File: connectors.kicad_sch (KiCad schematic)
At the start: 16 parts

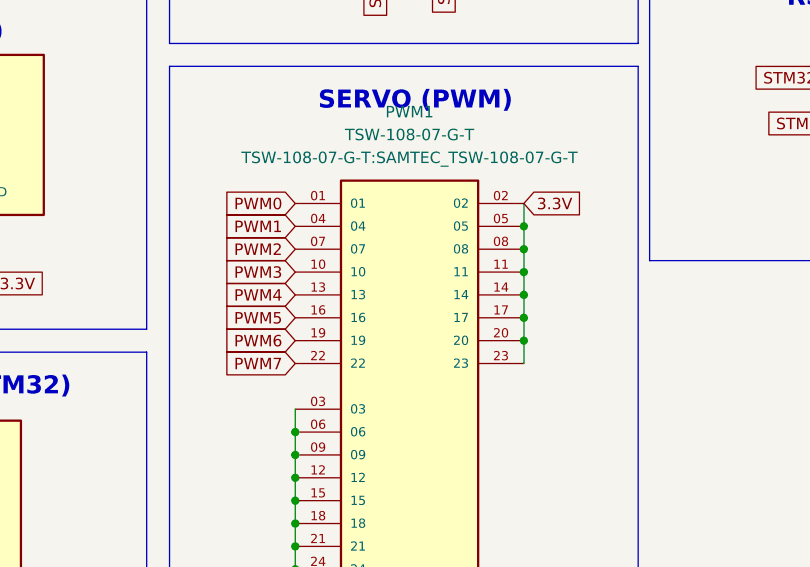
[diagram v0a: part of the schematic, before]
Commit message: grouped components
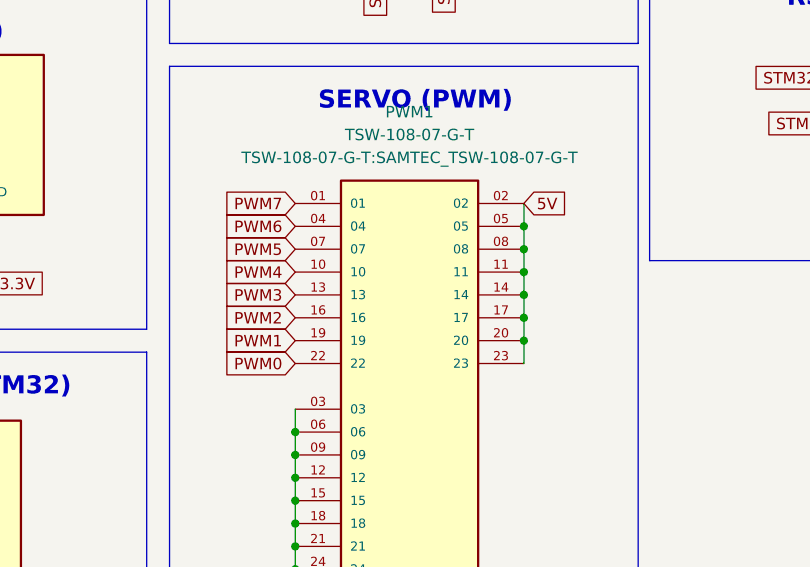
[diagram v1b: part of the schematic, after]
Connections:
- net 3.3V: no longer PWM1.02, PWM1.05, PWM1.08, PWM1.11, PWM1.14, PWM1.17, PWM1.20, PWM1.23
- net 5V: now also PWM1.02, PWM1.05, PWM1.08, PWM1.11, PWM1.14, PWM1.17, PWM1.20, PWM1.23
- net PWM0: now also PWM1.22; no longer PWM1.01
- net PWM1: now also PWM1.19; no longer PWM1.04
- net PWM2: now also PWM1.16; no longer PWM1.07
- net PWM3: now also PWM1.13; no longer PWM1.10
- net PWM4: now also PWM1.10; no longer PWM1.13
- net PWM5: now also PWM1.07; no longer PWM1.16
- net PWM6: now also PWM1.04; no longer PWM1.19
- net PWM7: now also PWM1.01; no longer PWM1.22

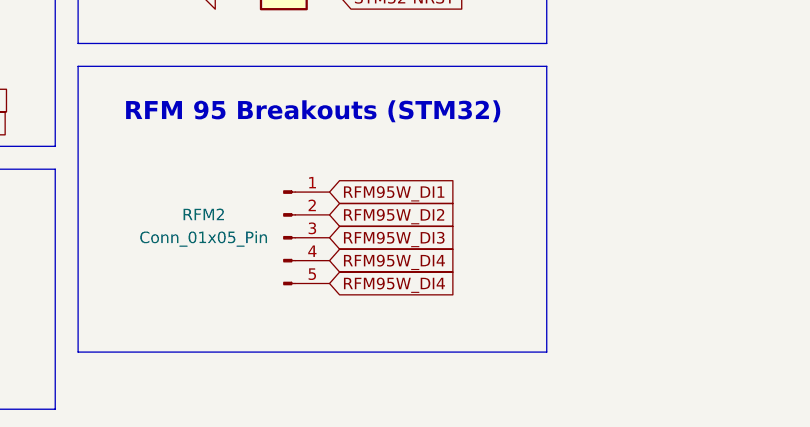
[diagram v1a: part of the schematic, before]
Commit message: updated tracks
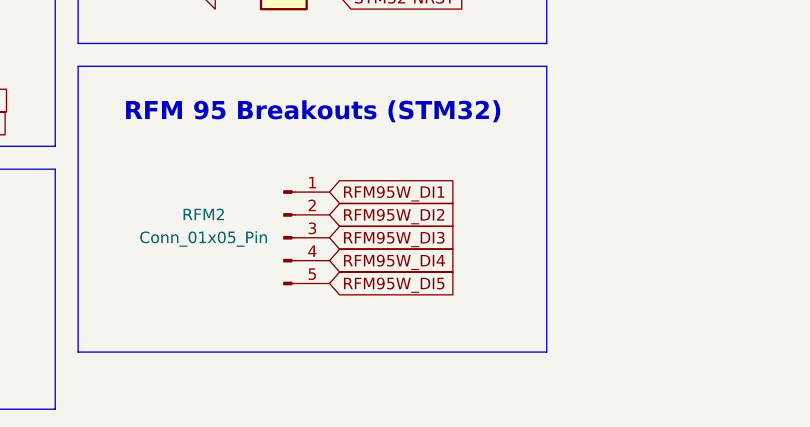
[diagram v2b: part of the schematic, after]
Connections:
- net RFM95W_DI4: no longer RFM2.5 (Pin_5)
- new net RFM95W_DI5: RFM2.5 (Pin_5)
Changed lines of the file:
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@@
     )
   )
-  (global_label "RFM95W_DI4" (shape input) (at 97.79 181.61 0) (fields_autoplaced)
+  (global_label "RFM95W_DI5" (shape input) (at 97.79 181.61 0) (fields_autoplaced)
     (effects (font (size 1.27 1.27)) (justify left))
     (property "Intersheetrefs" "${INTERSHEET_REFS}" (at 112.5075 181.61 0)

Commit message: started routing
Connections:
- net PWM0: now also PWM1.01; no longer PWM1.22
- net PWM1: now also PWM1.04; no longer PWM1.19
- net PWM2: now also PWM1.07; no longer PWM1.16
- net PWM3: now also PWM1.10; no longer PWM1.13
- net PWM4: now also PWM1.13; no longer PWM1.10
- net PWM5: now also PWM1.16; no longer PWM1.07
- net PWM6: now also PWM1.19; no longer PWM1.04
- net PWM7: now also PWM1.22; no longer PWM1.01
- net RFM95W_DI1: now also RFM2.5 (Pin_5); no longer RFM2.1 (Pin_1)
- net RFM95W_DI2: now also RFM2.4 (Pin_4); no longer RFM2.2 (Pin_2)
- net RFM95W_DI4: now also RFM2.2 (Pin_2); no longer RFM2.4 (Pin_4)
- net RFM95W_DI5: now also RFM2.1 (Pin_1); no longer RFM2.5 (Pin_5)
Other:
- moved on the sheet: RFM2

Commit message: more routing
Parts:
- added J2: Screw_Terminal_01x04, TerminalBlock_TE-Connectivity:TerminalBlock_TE_282834-4_1x04_P2.54mm_Horizontal, symbol Connector:Screw_Terminal_01x04
- added RFM3: Conn_01x05_Pin, Connector_PinHeader_1.27mm:PinHeader_1x05_P1.27mm_Vertical, symbol Connector:Conn_01x05_Pin
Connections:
- new net GPS_INT: RFM3.4 (Pin_4)
- new net GPS_RST: RFM3.3 (Pin_3)
- new net GPS_RX: RFM3.1 (Pin_1)
- new net GPS_SAFE: RFM3.5 (Pin_5)
- new net GPS_TX: RFM3.2 (Pin_2)
- new net PYRO-TERM_A: J2.1 (Pin_1)
- new net PYRO-TERM_B: J2.2 (Pin_2)
- new net PYRO-TERM_C: J2.3 (Pin_3)
- new net PYRO-TERM_D: J2.4 (Pin_4)
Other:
- note added: "GPS Breakouts"
- note added: "PYRO (STM32)"
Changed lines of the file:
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@@
+    (fill (type none))
+  )
+  (rectangle (start 124.46 124.46) (end 176.53 156.21)
+    (stroke (width 0) (type default))
     (fill (type none))
   )
@@
     (fill (type none))
   )
+  (rectangle (start 124.46 83.82) (end 185.42 121.92)
+    (stroke (width 0) (type default))
+    (fill (type none))
+  )
   (rectangle (start 69.85 60.96) (end 121.92 121.92)
     (stroke (width 0) (type default))
@@
     (effects (font (size 2 2) (thickness 0.8) bold) (justify left bottom))
   )
+  (text "PYRO (STM32)" (at 138.43 90.17 0)
+    (effects (font (size 2 2) (thickness 0.8) bold) (justify left bottom))
+  )
   (text "SWD Connector (STM32)" (at 78.74 129.54 0)
     (effects (font (size 2 2) (thickness 0.8) bold) (justify left bottom))
@@
     (effects (font (size 1.27 1.27) bold) (justify left bottom))
   )
+  (text "GPS Breakouts\n" (at 138.43 129.54 0)
+    (effects (font (size 2 2) (thickness 0.8) bold) (justify left bottom))
+  )
   (text "RFD UART 1 (STM32)" (at 26.67 97.79 0)
     (effects (font (size 2 2) (thickness 0.8) bold) (justify left bottom))
@@
     )
   )
+  (global_label "GPS_RX" (shape input) (at 149.86 134.62 0) (fields_autoplaced)
+    (effects (font (size 1.27 1.27)) (justify left))
+    (property "Intersheetrefs" "${INTERSHEET_REFS}" (at 160.0418 134.62 0)
+      (effects (font (size 1.27 1.27)) (justify left) hide)
+    )
+  )
   (global_label "ESP32-I2C1_SCL" (shape input) (at 41.91 86.36 180) (fields_autoplaced)
     (effects (font (size 1.27 1.27)) (justify right))
@@
     )
   )
+  (global_label "GPS_TX" (shape input) (at 149.86 137.16 0) (fields_autoplaced)
+    (effects (font (size 1.27 1.27)) (justify left))
+    (property "Intersheetrefs" "${INTERSHEET_REFS}" (at 159.7394 137.16 0)
+      (effects (font (size 1.27 1.27)) (justify left) hide)
+    )
+  )
   (global_label "INA219_SCL" (shape input) (at 251.46 53.34 0) (fields_autoplaced)
     (effects (font (size 1.27 1.27)) (justify left))
@@
     )
   )
+  (global_label "GPS_SAFE" (shape input) (at 149.86 144.78 0) (fields_autoplaced)
+    (effects (font (size 1.27 1.27)) (justify left))
+    (property "Intersheetrefs" "${INTERSHEET_REFS}" (at 162.098 144.78 0)
+      (effects (font (size 1.27 1.27)) (justify left) hide)
+    )
+  )
+  (global_label "PYRO-TERM_C" (shape input) (at 152.4 102.87 180) (fields_autoplaced)
+    (effects (font (size 1.27 1.27)) (justify right))
+    (property "Intersheetrefs" "${INTERSHEET_REFS}" (at 135.8077 102.87 0)
+      (effects (font (size 1.27 1.27)) (justify right) hide)
+    )
+  )
   (global_label "ESP32_RFD900_TX" (shape input) (at 40.64 148.59 180) (fields_autoplaced)
     (effects (font (size 1.27 1.27)) (justify right))
@@
     )
   )
+  (global_label "PYRO-TERM_A" (shape input) (at 152.4 97.79 180) (fields_autoplaced)
+    (effects (font (size 1.27 1.27)) (justify right))
+    (property "Intersheetrefs" "${INTERSHEET_REFS}" (at 135.9891 97.79 0)
+      (effects (font (size 1.27 1.27)) (justify right) hide)
+    )
+  )
   (global_label "H3LIS331DL_SDO" (shape input) (at 255.27 106.68 0) (fields_autoplaced)
     (effects (font (size 1.27 1.27)) (justify left))
@@
     )
   )
+  (global_label "PYRO-TERM_B" (shape input) (at 152.4 100.33 180) (fields_autoplaced)
+    (effects (font (size 1.27 1.27)) (justify right))
+    (property "Intersheetrefs" "${INTERSHEET_REFS}" (at 135.8077 100.33 0)
+      (effects (font (size 1.27 1.27)) (justify right) hide)
+    )
+  )
   (global_label "SD_CS" (shape input) (at 255.27 135.89 0) (fields_autoplaced)
     (effects (font (size 1.27 1.27)) (justify left))
@@
     )
   )
+  (global_label "GPS_INT" (shape input) (at 149.86 142.24 0) (fields_autoplaced)
+    (effects (font (size 1.27 1.27)) (justify left))
+    (property "Intersheetrefs" "${INTERSHEET_REFS}" (at 160.4652 142.24 0)
+      (effects (font (size 1.27 1.27)) (justify left) hide)
+    )
+  )
   (global_label "STM32-SPI2_CS0" (shape input) (at 250.19 124.46 180) (fields_autoplaced)
     (effects (font (size 1.27 1.27)) (justify right))
@@
     )
   )
+  (global_label "PYRO-TERM_D" (shape input) (at 152.4 105.41 180) (fields_autoplaced)
+    (effects (font (size 1.27 1.27)) (justify right))
+    (property "Intersheetrefs" "${INTERSHEET_REFS}" (at 135.8077 105.41 0)
+      (effects (font (size 1.27 1.27)) (justify right) hide)
+    )
+  )
   (global_label "5V" (shape input) (at 40.64 105.41 180) (fields_autoplaced)
     (effects (font (size 1.27 1.27)) (justify right))
@@
     (property "Intersheetrefs" "${INTERSHEET_REFS}" (at 233.1745 158.75 0)
       (effects (font (size 1.27 1.27)) (justify right) hide)
+    )
+  )
+  (global_label "GPS_RST" (shape input) (at 149.86 139.7 0) (fields_autoplaced)
+    (effects (font (size 1.27 1.27)) (justify left))
+    (property "Intersheetrefs" "${INTERSHEET_REFS}" (at 161.0094 139.7 0)
+      (effects (font (size 1.27 1.27)) (justify left) hide)
     )
   )
@@
         (path "/e12346fa-509d-4de9-8ab1-dced307292db/7d58c90a-6730-4b63-ae17-c9d1fe4b2f54"
           (reference "#PWR0166") (unit 1)
+        )
+      )
+    )
+  )
+  (symbol (lib_id "Connector:Conn_01x05_Pin") (at 144.78 139.7 0) (unit 1)
+    (in_bom yes) (on_board yes) (dnp no)
+    (property "Reference" "RFM3" (at 135.89 137.16 0)
+      (effects (font (size 1.27 1.27)))
+    )
+    (property "Value" "Conn_01x05_Pin" (at 135.89 139.7 0)
+      (effects (font (size 1.27 1.27)))
+    )
+    (property "Footprint" "Connector_PinHeader_1.27mm:PinHeader_1x05_P1.27mm_Vertical" (at 144.78 139.7 0)
+      (effects (font (size 1.27 1.27)) hide)
+    )
+    (property "Datasheet" "~" (at 144.78 139.7 0)
+      (effects (font (size 1.27 1.27)) hide)
+    )
+    (pin "1")
+    (pin "2")
+    (pin "3")
+    (pin "4")
+    (pin "5")
+    (instances
+      (project "aether"
+        (path "/e12346fa-509d-4de9-8ab1-dced307292db/7d58c90a-6730-4b63-ae17-c9d1fe4b2f54"
+          (reference "RFM3") (unit 1)
         )
       )
@@
         )
       )
+    )
+  )
+  (symbol (lib_id "Connector:Screw_Terminal_01x04") (at 157.48 100.33 0) (unit 1)
+    (in_bom yes) (on_board yes) (dnp no) (fields_autoplaced)
+    (property "Reference" "J2" (at 160.02 100.33 0)
+      (effects (font (size 1.27 1.27)) (justify left))
+    )
+    (property "Value" "Screw_Terminal_01x04" (at 160.02 102.87 0)
+      (effects (font (size 1.27 1.27)) (justify left))
+    )
+    (property "Footprint" "TerminalBlock_TE-Connectivity:TerminalBlock_TE_282834-4_1x04_P2.54mm_Horizontal" (at 157.48 100.33 0)
+      (effects (font (size 1.27 1.27)) hide)
+    )
+    (property "Datasheet" "~" (at 157.48 100.33 0)
+      (effects (font (size 1.27 1.27)) hide)
+    )
+    (pin "1")
+    (pin "2")
+    (pin "3")
+    (pin "4")
+    (instances
+      (project "aether"
+        (path "/e12346fa-509d-4de9-8ab1-dced307292db/7d58c90a-6730-4b63-ae17-c9d1fe4b2f54"
+          (reference "J2") (unit 1)
+        )
+      )

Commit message: significant amount of routing done
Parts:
- R? (x2): footprint Resistor_SMD:R_0603_1608Metric -> Resistor_SMD:R_0402_1005Metric
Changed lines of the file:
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@@
       (effects (font (size 1.27 1.27)))
     )
-    (property "Footprint" "Resistor_SMD:R_0603_1608Metric" (at 45.72 85.598 90)
+    (property "Footprint" "Resistor_SMD:R_0402_1005Metric" (at 45.72 85.598 90)
       (effects (font (size 1.27 1.27)) hide)
     )
@@
       (effects (font (size 1.27 1.27)))
     )
-    (property "Footprint" "Resistor_SMD:R_0603_1608Metric" (at 45.72 88.138 90)
-      (effects (font (size 1.27 1.27)) hide)
-    )
+    (property "Footprint" "Resistor_SMD:R_0402_1005Metric" (at 45.72 88.138 90)
+      (effects (font (size 1.27 1.27)) hide)
+    )

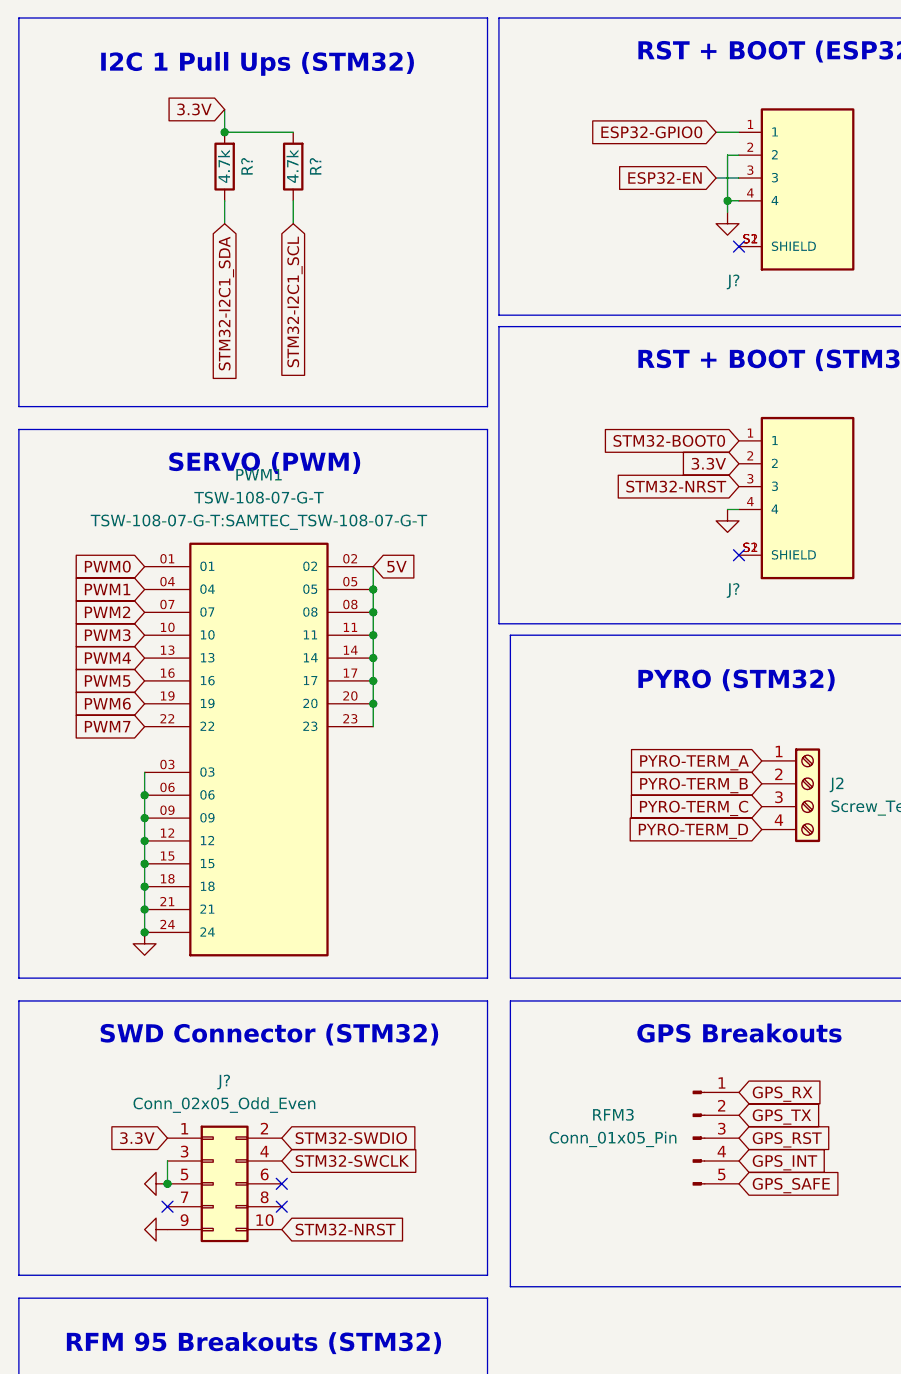
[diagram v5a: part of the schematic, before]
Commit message: signals routed
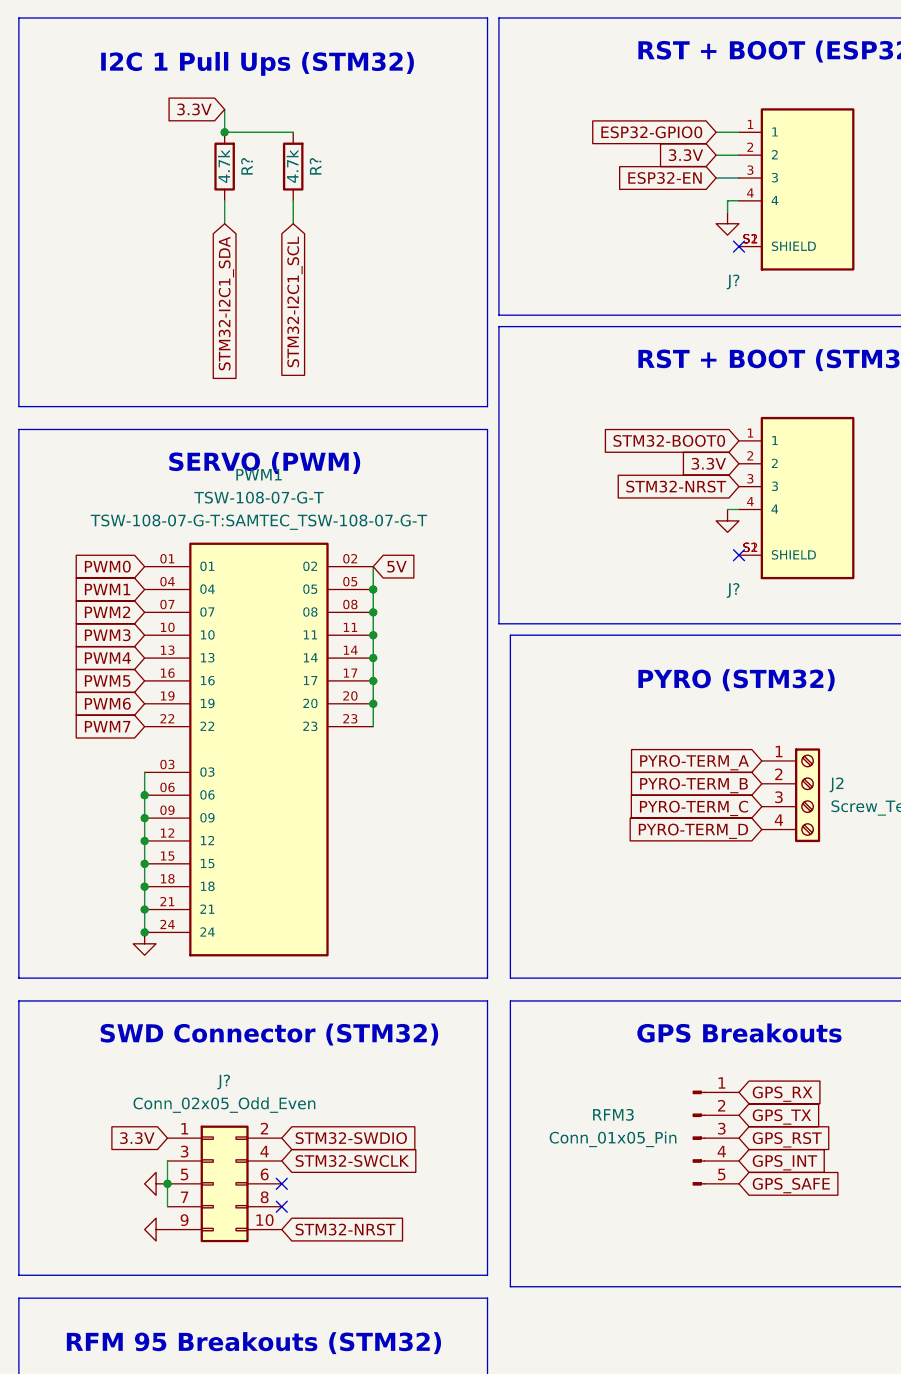
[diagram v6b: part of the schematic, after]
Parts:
- R? (x2): footprint Resistor_SMD:R_0603_1608Metric -> Resistor_SMD:R_0402_1005Metric
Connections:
- net 3.3V: now also J?.2
- net GND: now also J?.7 (Pin_7); no longer J?.2
- no-connect marks 10 -> 9
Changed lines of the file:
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@@
   (junction (at 83.82 104.14) (diameter 0) (color 0 0 0 0)
-  )
-  (junction (at 148.59 35.56) (diameter 0) (color 0 0 0 0)
   )
   (junction (at 83.82 111.76) (diameter 0) (color 0 0 0 0)
@@
   (no_connect (at 43.18 35.56))
   (no_connect (at 149.86 40.64))
-  (no_connect (at 86.36 147.32))
   (no_connect (at 43.18 74.93))
   (no_connect (at 40.64 153.67))
@@
     (stroke (width 0) (type default))
   )
-  (wire (pts (xy 148.59 30.48) (xy 148.59 35.56))
-    (stroke (width 0) (type default))
-  )
   (wire (pts (xy 255.27 101.6) (xy 250.19 101.6))
     (stroke (width 0.5) (type solid) (color 255 0 0 1))
@@
     (stroke (width 0.5) (type solid) (color 255 0 0 1))
   )
-  (wire (pts (xy 149.86 30.48) (xy 148.59 30.48))
+  (wire (pts (xy 149.86 30.48) (xy 147.32 30.48))
     (stroke (width 0) (type default))
   )
@@
   (wire (pts (xy 255.27 101.6) (xy 255.27 109.22))
     (stroke (width 0.5) (type solid) (color 255 0 0 1))
+  )
+  (wire (pts (xy 86.36 144.78) (xy 86.36 147.32))
+    (stroke (width 0) (type default))
   )
   (wire (pts (xy 45.72 125.73) (xy 40.64 125.73))
@@
     (effects (font (size 1.27 1.27)) (justify right))
     (property "Intersheetrefs" "${INTERSHEET_REFS}" (at 232.2673 151.13 0)
+      (effects (font (size 1.27 1.27)) (justify right) hide)
+    )
+  )
+  (global_label "3.3V" (shape input) (at 147.32 30.48 180) (fields_autoplaced)
+    (effects (font (size 1.27 1.27)) (justify right))
+    (property "Intersheetrefs" "${INTERSHEET_REFS}" (at 140.2224 30.48 0)
       (effects (font (size 1.27 1.27)) (justify right) hide)
     )
@@
       (effects (font (size 1.27 1.27)))
     )
-    (property "Footprint" "Resistor_SMD:R_0603_1608Metric" (at 45.72 46.228 90)
+    (property "Footprint" "Resistor_SMD:R_0402_1005Metric" (at 45.72 46.228 90)
       (effects (font (size 1.27 1.27)) hide)
     )
@@
       (effects (font (size 1.27 1.27)))
     )
-    (property "Footprint" "Resistor_SMD:R_0603_1608Metric" (at 45.72 48.768 90)
-      (effects (font (size 1.27 1.27)) hide)
-    )
+    (property "Footprint" "Resistor_SMD:R_0402_1005Metric" (at 45.72 48.768 90)
+      (effects (font (size 1.27 1.27)) hide)
+    )
